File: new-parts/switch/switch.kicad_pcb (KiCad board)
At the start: 2 copper layers, 63.5 x 38.1 mm, 26 parts, among them J1 Conn_02x02_Odd_Even, J2 BHR-10-VUA, SW1 SW_SPDT, SW2 SW_SPDT, SW3 SW_SPDT, SW4 SW_SPDT, SW5 SW_SPDT, SW6 SW_SPDT, SW7 SW_SPDT, SW8 SW_SPDT

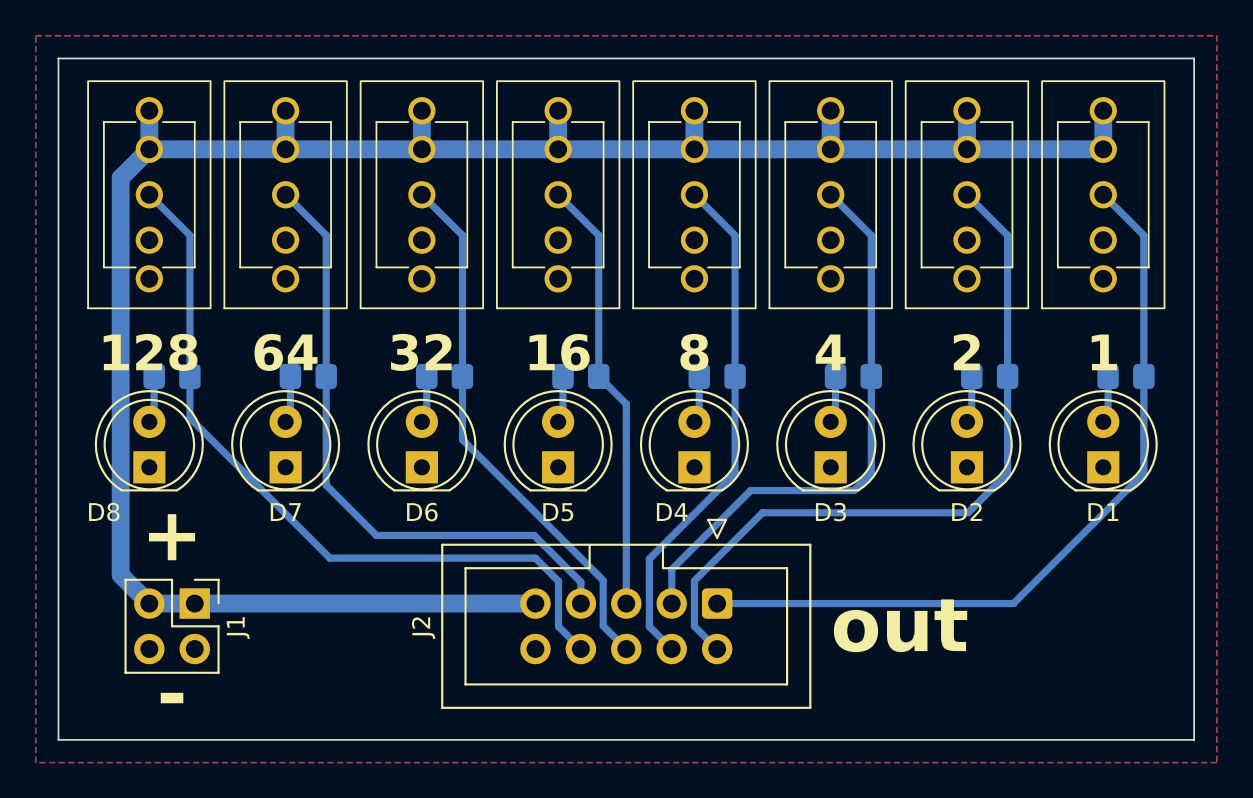
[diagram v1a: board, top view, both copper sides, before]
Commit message: switch: Fix footprint so that the larger pins fit.
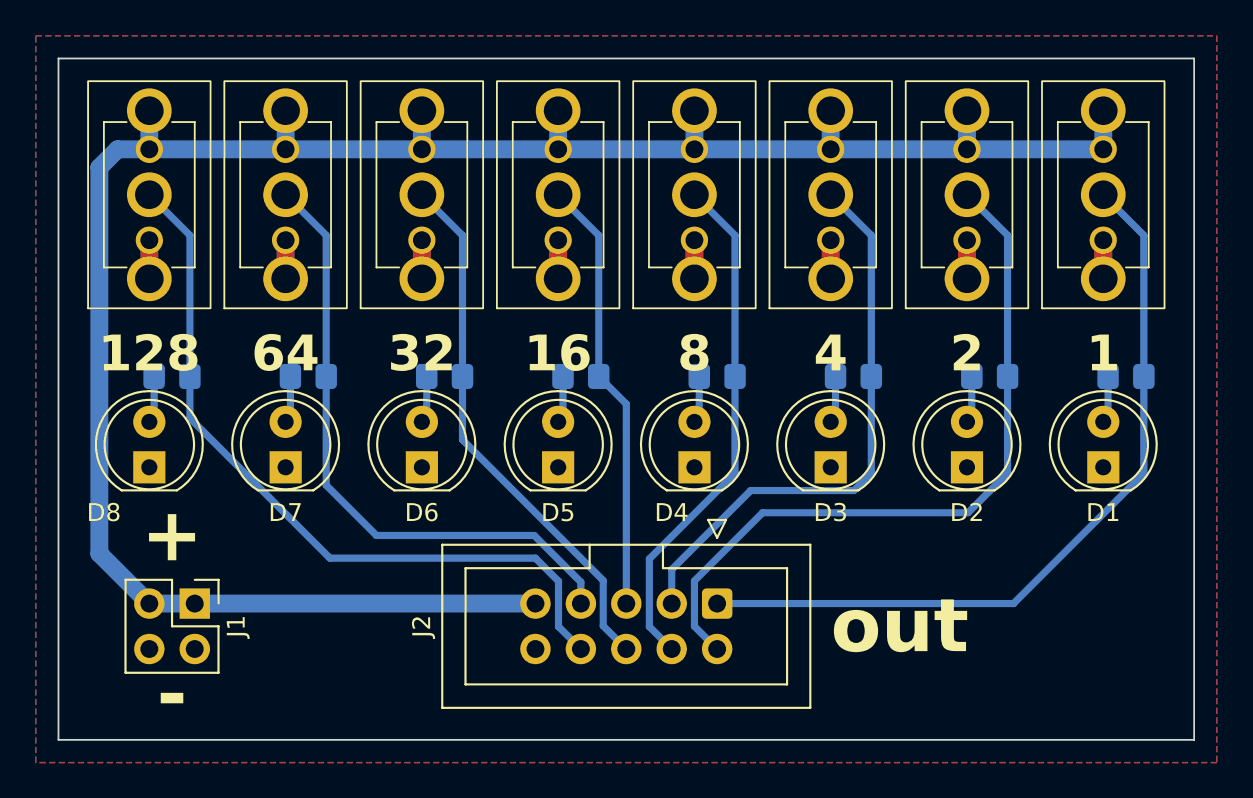
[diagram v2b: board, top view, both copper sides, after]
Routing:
- net GND: track 0.00 -> 17.3 mm
- net VCC: track 118.9 -> 121.0 mm

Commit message: Add "r2" to updated PCBs.
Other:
- board text added: "r2"
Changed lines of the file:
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@@
 		(layer "Edge.Cuts")
+	)
+	(gr_text "\nr2"
+		(at 156.845 104.14 0)
+		(layer "B.SilkS")
+		(effects
+			(font
+				(size 3 3)
+				(thickness 0.6)
+				(bold yes)
+			)
+			(justify left mirror)
+		)
 	)
 	(gr_text "vis vitalis \nswitches"
